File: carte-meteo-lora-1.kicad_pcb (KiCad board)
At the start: 2 copper layers, 60 x 45 mm, 121 parts, among them J1 TC2030, J2 Conn_01x04, J3 Conn_01x04, J4 Conn_Coaxial, J5 USB_C_Receptacle_USB2.0_14P, J6 Solar_Cell, J7 Conn_01x02, J8 Battery_Cell, Q1 AO4882, Q2 AO4882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

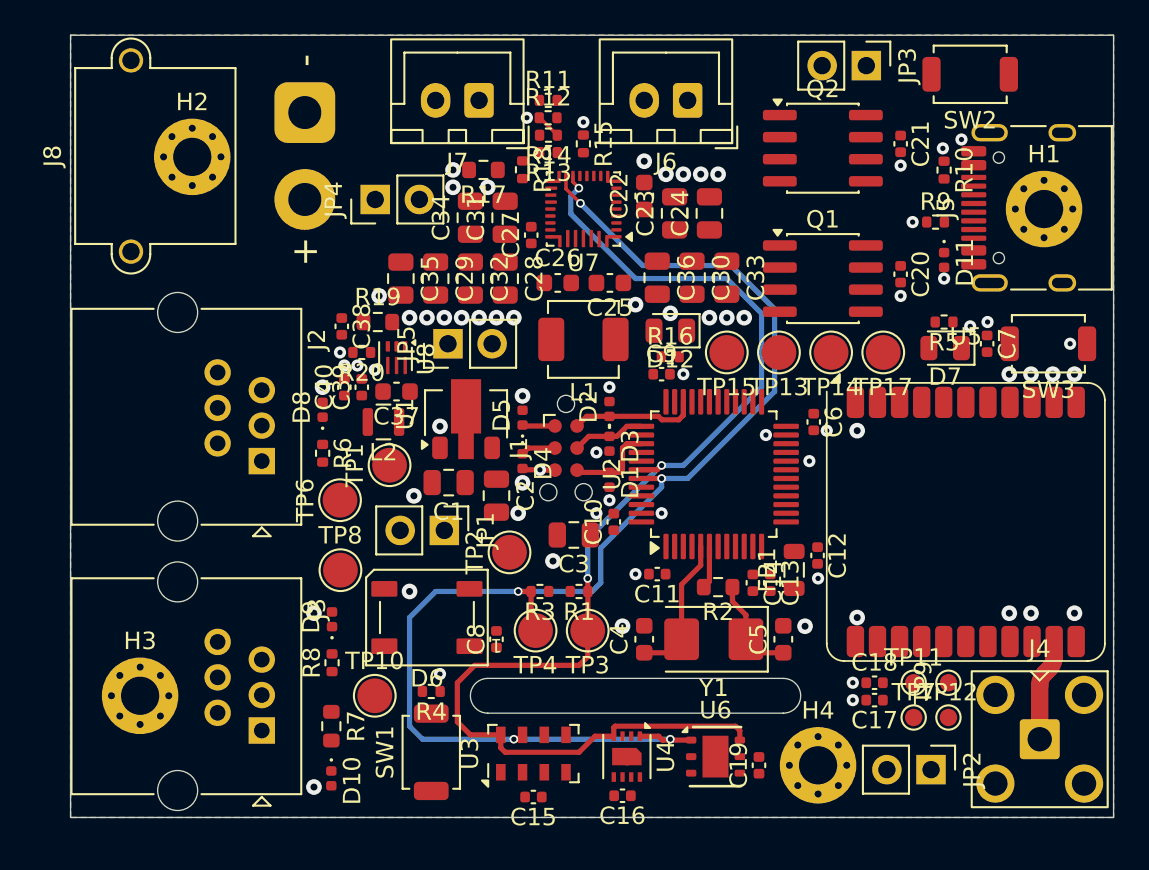
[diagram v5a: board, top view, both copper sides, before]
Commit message: pcb: add solar charger routing
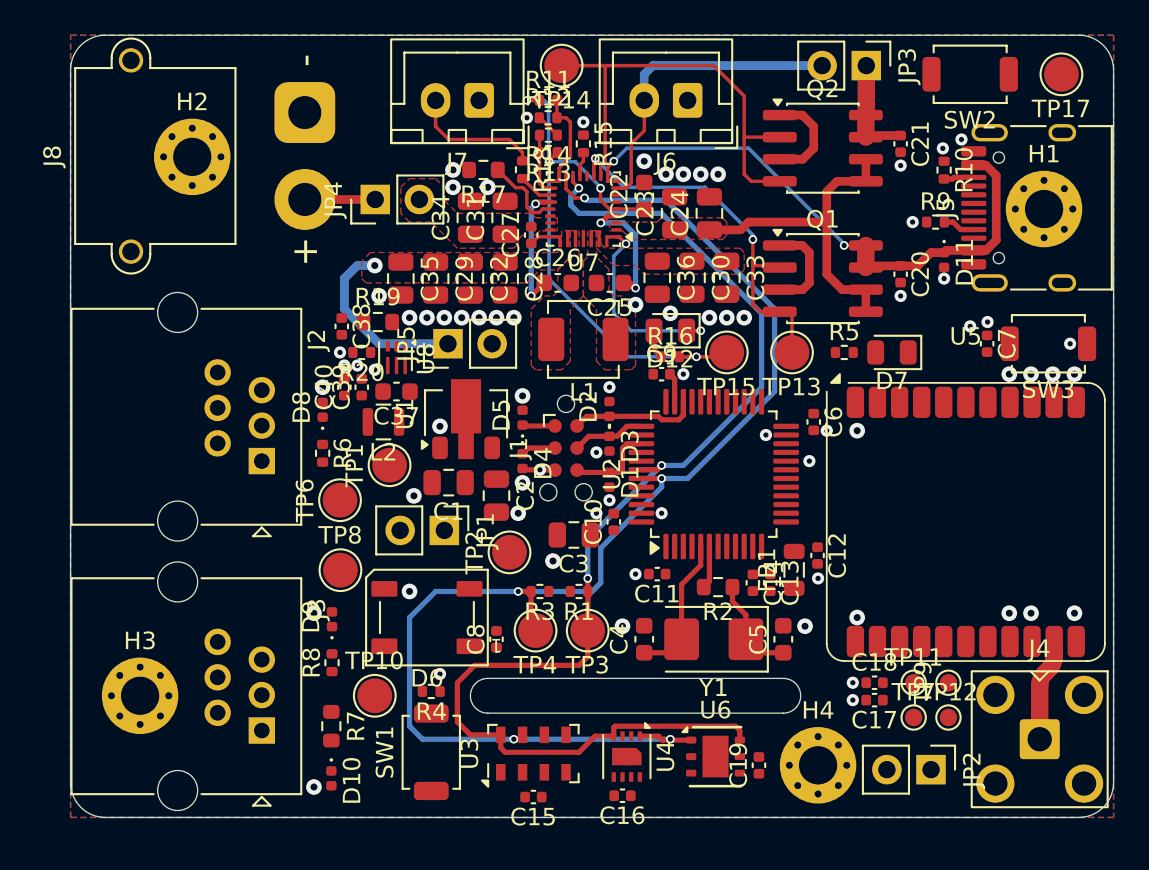
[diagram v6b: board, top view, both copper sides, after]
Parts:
- moved TP14 22.6 mm to (78.2, 24.8)
- moved TP17 19.0 mm to (107.0, 25.2)
- moved R5 6.00 mm to (94.5, 41.2), turned to 0 degrees
- moved D7 3.07 mm to (97.2, 41.2)
- moved TP13 0.75 mm to (91.5, 41.2)
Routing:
- net +REGN: track 0.00 -> 33.1 mm, vias 0 -> 4
- net +Vbus: track 0.00 -> 32.9 mm, vias 0 -> 2
- net Net-(Q2A-G1): track 0.00 -> 26.4 mm
- net Net-(J6--): track 0.00 -> 24.1 mm
- net Net-(Q1A-G1): track 0.00 -> 22.2 mm, vias 0 -> 2
- net Net-(C23-Pad1): track 0.00 -> 19.3 mm
- net Net-(D12-K): track 0.00 -> 11.2 mm, vias 0 -> 2
- net +SYS: track 0.00 -> 10.6 mm, vias 0 -> 1
- net Net-(J7-Pin_2): track 0.00 -> 7.60 mm
- net Net-(U7-BTST2): track 0.00 -> 7.39 mm, vias 0 -> 2
- net Net-(U7-BTST1): track 0.00 -> 7.23 mm, vias 0 -> 2
- net Net-(U7-TS): track 0.00 -> 5.98 mm
- net Net-(Q2A-S1): track 0.00 -> 5.68 mm
- net Net-(Q1A-S1): track 0.00 -> 5.48 mm
- net Net-(U7-PROG): track 0.00 -> 4.65 mm
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- added copper zone on F.Cu, net +SYS
- added copper zone on F.Cu, net Net-(C23-Pad1)
- added copper zone on F.Cu, net Net-(J8--)
- added copper zone on F.Cu, net Net-(U7-PMID)
- added copper zone on F.Cu, net Net-(U7-SW1)
- added copper zone on F.Cu, net Net-(U7-SW2)
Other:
- outline, holes or cut-outs redrawn

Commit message: pcb: add lora spi routing
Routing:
- net /CS: track 0.00 -> 21.0 mm, vias 0 -> 2
- net /MOSI: track 0.00 -> 21.0 mm
- net /SCK: track 0.00 -> 17.1 mm
- net /MISO: track 0.00 -> 16.7 mm
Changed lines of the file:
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@@
+	)
+	(segment
+		(start 96.75 49)
+		(end 91.1625 49)
+		(width 0.3)
+		(layer "F.Cu")
+		(net "/MOSI")
+	)
+	(segment
+		(start 99.5 59.75)
+		(end 100.23 59.02)
+		(width 0.3)
+		(layer "F.Cu")
+		(net "/MOSI")
+	)
+	(segment
+		(start 100.23 59.02)
+		(end 100.23 57.88)
+		(width 0.3)
+		(layer "F.Cu")
+		(net "/MOSI")
+	)
+	(segment
+		(start 99.5 61.25)
+		(end 99.5 59.75)
+		(width 0.3)
+		(layer "F.Cu")
+		(net "/MOSI")
+	)
+	(segment
+		(start 100.23 52.48)
+		(end 96.75 49)
+		(width 0.3)
+		(layer "F.Cu")
+		(net "/MOSI")
+	)
+	(segment
+		(start 100.23 57.88)
+		(end 100.23 52.48)
+		(width 0.3)
+		(layer "F.Cu")
+		(net "/MOSI")
+	)
+	(segment
+		(start 100.5 62.25)
+		(end 99.5 61.25)
+		(width 0.3)
+		(layer "F.Cu")
+		(net "/MOSI")
+	)
+	(segment
+		(start 98.96 52.96)
+		(end 95.5 49.5)
+		(width 0.3)
+		(layer "F.Cu")
+		(net "/MISO")
+	)
+	(segment
+		(start 98.96 57.88)
+		(end 98.96 59.79)
+		(width 0.3)
+		(layer "F.Cu")
+		(net "/MISO")
+	)
+	(segment
+		(start 95.5 49.5)
+		(end 91.1625 49.5)
+		(width 0.3)
+		(layer "F.Cu")
+		(net "/MISO")
+	)
+	(segment
+		(start 98.96 59.79)
+		(end 98.5 60.25)
+		(width 0.3)
+		(layer "F.Cu")
+		(net "/MISO")
+	)
+	(segment
+		(start 98.96 57.88)
+		(end 98.96 52.96)
+		(width 0.3)
+		(layer "F.Cu")
+		(net "/MISO")
 	)
 	(segment
@@
 	)
 	(segment
+		(start 94.25 50)
+		(end 91.1625 50)
+		(width 0.3)
+		(layer "F.Cu")
+		(net "/SCK")
+	)
+	(segment
+		(start 97.69 57.88)
+		(end 97.69 53.44)
+		(width 0.3)
+		(layer "F.Cu")
+		(net "/SCK")
+	)
+	(segment
+		(start 97.69 57.88)
+		(end 97.69 61.44)
+		(width 0.3)
+		(layer "F.Cu")
+		(net "/SCK")
+	)
+	(segment
+		(start 97.69 53.44)
+		(end 94.25 50)
+		(width 0.3)
+		(layer "F.Cu")
+		(net "/SCK")
+	)
+	(segment
+		(start 97.69 61.44)
+		(end 98.5 62.25)
+		(width 0.3)
+		(layer "F.Cu")
+		(net "/SCK")
+	)
+	(segment
+		(start 101.5 59.25)
+		(end 101.5 57.88)
+		(width 0.3)
+		(layer "F.Cu")
+		(net "/CS")
+	)
+	(segment
+		(start 100.5 60.25)
+		(end 101.5 59.25)
+		(width 0.3)
+		(layer "F.Cu")
+		(net "/CS")
+	)
+	(segment
+		(start 96.5 53.5)
+		(end 96.5 56.25)
+		(width 0.3)
+		(layer "F.Cu")
+		(net "/CS")
+	)
+	(segment
+		(start 101.5 56.5)
+		(end 101.5 57.88)
+		(width 0.3)
+		(layer "F.Cu")
+		(net "/CS")
+	)
+	(segment
+		(start 91.1625 50.5)
+		(end 93.5 50.5)
+		(width 0.3)
+		(layer "F.Cu")
+		(net "/CS")
+	)
+	(segment
+		(start 93.5 50.5)
+		(end 96.5 53.5)
+		(width 0.3)
+		(layer "F.Cu")
+		(net "/CS")
+	)
+	(via
+		(at 96.5 56.25)
+		(size 0.5)
+		(drill 0.3)
+		(layers "F.Cu" "B.Cu")
+		(net "/CS")
+	)
+	(via
+		(at 101.5 56.5)
+		(size 0.5)
+		(drill 0.3)
+		(layers "F.Cu" "B.Cu")
+		(net "/CS")
+	)
+	(segment
+		(start 101.5 57.25)
+		(end 101.5 56.5)
+		(width 0.3)
+		(layer "B.Cu")
+		(net "/CS")
+	)
+	(segment
+		(start 96.5 56.25)
+		(end 96.5 57.5)
+		(width 0.3)
+		(layer "B.Cu")
+		(net "/CS")
+	)
+	(segment
+		(start 96.5 57.5)
+		(end 97 58)
+		(width 0.3)
+		(layer "B.Cu")
+		(net "/CS")
+	)
+	(segment
+		(start 100.75 58)
+		(end 101.5 57.25)
+		(width 0.3)
+		(layer "B.Cu")
+		(net "/CS")
+	)
+	(segment
+		(start 97 58)
+		(end 100.75 58)
+		(width 0.3)
+		(layer "B.Cu")
+		(net "/CS")
+	)
+	(segment

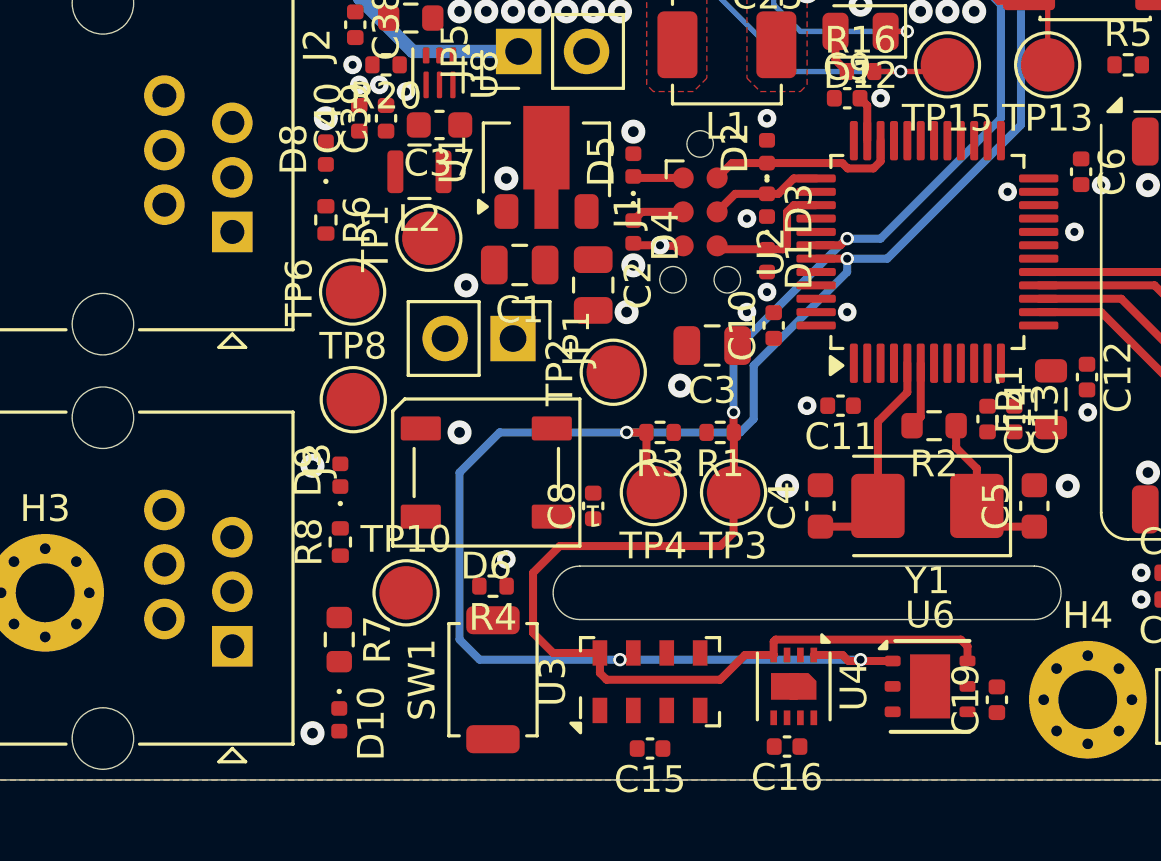
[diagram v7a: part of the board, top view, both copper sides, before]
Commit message: pcb: add rain/wind connectors routing
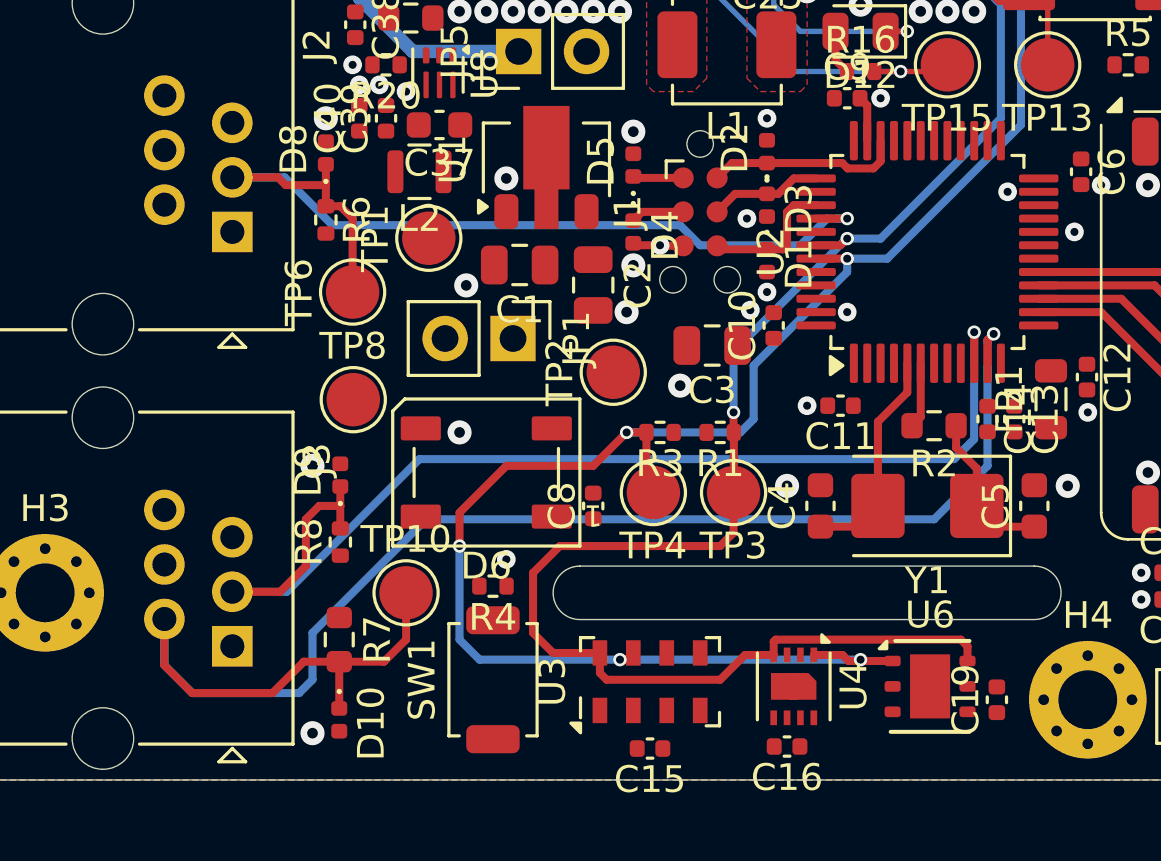
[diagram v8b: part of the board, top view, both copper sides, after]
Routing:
- net /W_DIR: track 0.00 -> 59.2 mm, vias 0 -> 1
- net /WIND: track 0.00 -> 43.2 mm, vias 0 -> 1
- net /RAIN: track 0.00 -> 34.8 mm, vias 0 -> 1
- net /SDA: track 77.7 -> 76.8 mm, vias 5 -> 6
